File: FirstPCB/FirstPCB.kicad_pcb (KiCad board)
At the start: 2 copper layers, 50 x 30 mm, 5 parts, among them U1 STM32G0B1KETx

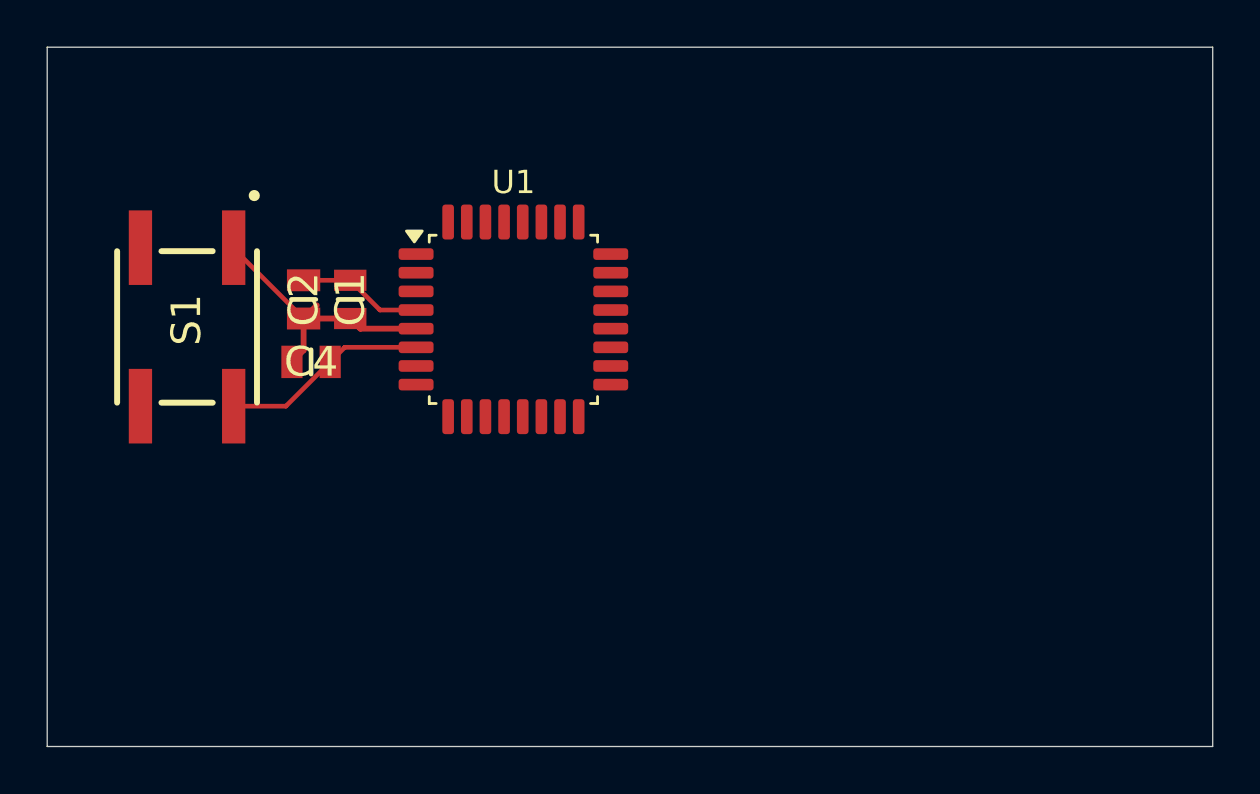
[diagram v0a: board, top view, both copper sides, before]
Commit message: added Voltage Regulator
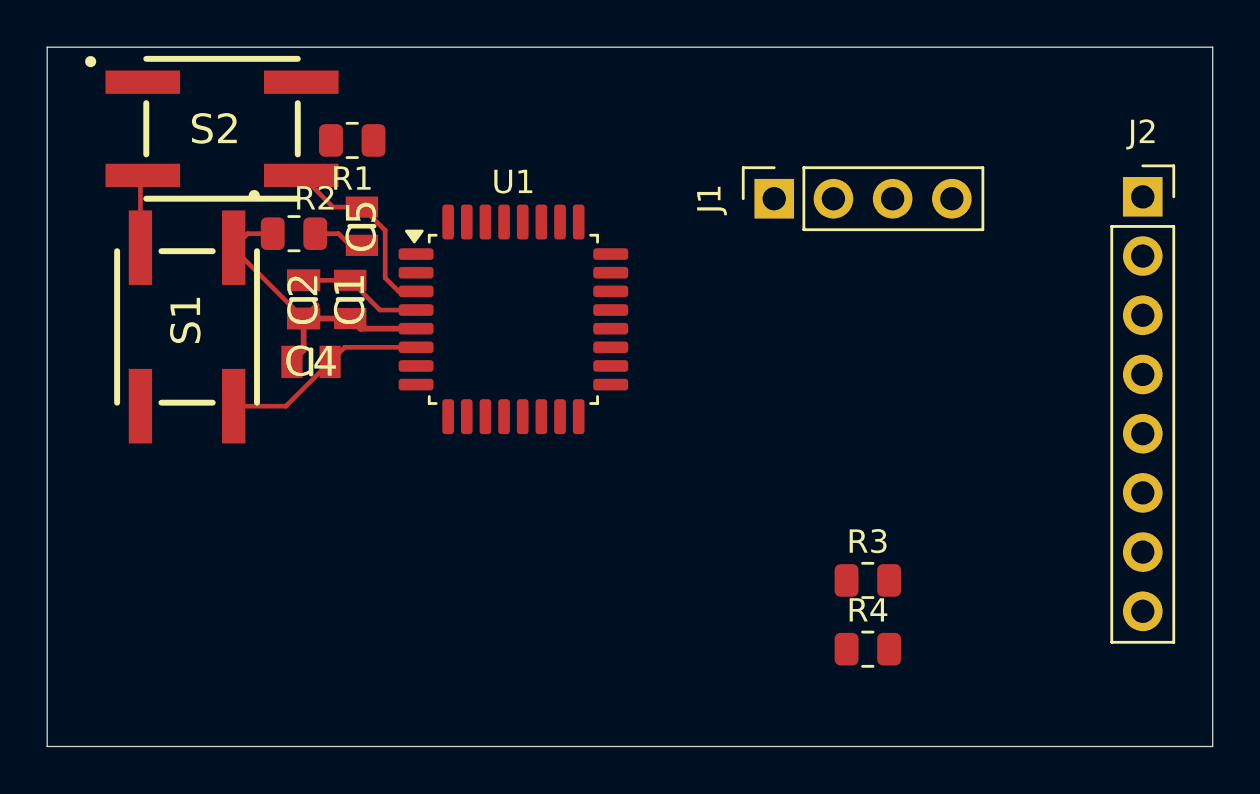
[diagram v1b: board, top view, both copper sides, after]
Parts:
- added C5: 100nF, SamacSys_Parts:CAPC2012X95N, F.Cu at (165.5, 89.7)
- added J1: Conn_01x04_Socket, Connector_PinSocket_2.54mm:PinSocket_1x04_P2.54mm_Vertical, F.Cu at (183.2, 88.5)
- added J2: Conn_01x08_Socket, Connector_PinSocket_2.54mm:PinSocket_1x08_P2.54mm_Vertical, F.Cu at (199.0, 88.4)
- added R1: 4.7 kOhm, Resistor_SMD:R_0805_2012Metric, F.Cu at (165.1, 86.0)
- added R2: 100 Ohm, Resistor_SMD:R_0805_2012Metric, F.Cu at (162.6, 90.0)
- added R3: 100 Ohm, Resistor_SMD:R_0805_2012Metric, F.Cu at (187.2, 104.9)
- added R4: 10 kOhm, Resistor_SMD:R_0805_2012Metric, F.Cu at (187.2, 107.8)
- added S2: EVQQ2B03W, SamacSys_Parts:EVQQ2, F.Cu at (159.5, 85.5)
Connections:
- U1 pad 23: unconnected-(U1-PA10/PA12-Pad23) -> Net-(U1-PA10/PA12)
- U1 pad 3: unconnected-(U1-PC15-Pad3) -> /BUTTON_CHANGE
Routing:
- net /BUTTON_CHANGE: track 0.00 -> 8.18 mm
- net GND: track 12.2 -> 17.2 mm
- net Net-(C5-Pad2): track 0.00 -> 2.21 mm
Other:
- board text added: "BUTTON_CHANGE"
- board text added: "N_RST"

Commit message: added sensor and schematic update
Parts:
- added R5: 1 kOhm, Resistor_SMD:R_0805_2012Metric, F.Cu at (186.7, 96.0)
- moved J1 1.69 mm to (181.5, 88.4), turned to 0 degrees
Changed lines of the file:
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@@
+		)
+	)
+	(footprint "Resistor_SMD:R_0805_2012Metric"
+		(layer "F.Cu")
+		(at 186.705 95.975)
+		(descr "Resistor SMD 0805 (2012 Metric), square (rectangular) end terminal, IPC-7351 nominal, (Body size source: IPC-SM-782 page 72, https://www.pcb-3d.com/wordpress/wp-content/uploads/ipc-sm-782a_amendment_1_and_2.pdf)")
+		(tags "resistor")
+		(property "Reference" "R5"
+			(at 0 -1.65 0)
+			(layer "F.SilkS")
+			(effects
+				(font
+					(size 1 1)
+					(thickness 0.15)
+				)
+			)
+		)
+		(property "Value" "1 kOhm"
+			(at 0 1.65 0)
+			(layer "F.Fab")
+			(effects
+				(font
+					(size 1 1)
+					(thickness 0.15)
+				)
+			)
+		)
+		(property "Datasheet" ""
+			(at 0 0 0)
+			(layer "F.Fab")
+			(hide yes)
+			(effects
+				(font
+					(size 1.27 1.27)
+				)
+			)
+		)
+		(property "Description" "Resistor"
+			(at 0 0 0)
+			(layer "F.Fab")
+			(hide yes)
+			(effects
+				(font
+					(size 1.27 1.27)
+				)
+			)
+		)
+		(property "KiLib_Generator" "SMD_2terminal_chip_molded"
+			(at 0 0 0)
+			(layer "F.SilkS")
+			(hide yes)
+			(effects
+				(font
+					(size 1 1)
+					(thickness 0.15)
+				)
+			)
+		)
+		(property ki_fp_filters "R_*")
+		(sheetname "/")
+		(sheetfile "FirstPCB.kicad_sch")
+		(units
+			(unit
+				(name "A")
+				(pins "1" "2")
+			)
+		)
+		(attr smd)
+		(duplicate_pad_numbers_are_jumpers no)
+		(fp_line
+			(start -0.227064 -0.735)
+			(end 0.227064 -0.735)
+			(stroke
+				(width 0.12)
+				(type solid)
+			)
+			(layer "F.SilkS")
+		)
+		(fp_line
+			(start -0.227064 0.735)
+			(end 0.227064 0.735)
+			(stroke
+				(width 0.12)
+				(type solid)
+			)
+			(layer "F.SilkS")
+		)
+		(fp_rect
+			(start -1.68 -0.95)
+			(end 1.68 0.95)
+			(stroke
+				(width 0.05)
+				(type solid)
+			)
+			(fill no)
+			(layer "F.CrtYd")
+		)
+		(fp_rect
+			(start -1 -0.625)
+			(end 1 0.625)
+			(stroke
+				(width 0.1)
+				(type solid)
+			)
+			(fill no)
+			(layer "F.Fab")
+		)
+		(fp_text user "${REFERENCE}"
+			(at 0 0 0)
+			(layer "F.Fab")
+			(effects
+				(font
+					(size 0.5 0.5)
+					(thickness 0.08)
+				)
+			)
+		)
+		(pad "1" smd roundrect
+			(at -0.9125 0)
+			(size 1.025 1.4)
+			(layers "F.Cu" "F.Mask" "F.Paste")
+			(roundrect_rratio 0.243902)
+			(net "+3.3V")
+			(pintype "passive")
+		)
+		(pad "2" smd roundrect
+			(at 0.9125 0)
+			(size 1.025 1.4)
+			(layers "F.Cu" "F.Mask" "F.Paste")
+			(roundrect_rratio 0.243902)
+			(net "Net-(LED1-Pad1)")
+			(pintype "passive")
+		)
+		(embedded_fonts no)
+		(model "${KICAD10_3DMODEL_DIR}/Resistor_SMD.3dshapes/R_0805_2012Metric.step"
+			(offset
+				(xyz 0 0 0)
+			)
+			(scale
+				(xyz 1 1 1)
+			)
+			(rotate
+				(xyz 0 0 0)
+			)
 		)
 	)
@@
 	(footprint "Connector_PinSocket_2.54mm:PinSocket_1x04_P2.54mm_Vertical"
 		(layer "F.Cu")
-		(at 183.19 88.5 90)
+		(at 181.5 88.42)
 		(descr "Through hole straight socket strip, 1x04, 2.54mm pitch, single row (from Kicad 4.0.7), script generated")
 		(tags "Through hole socket strip THT 1x04 2.54mm single row")
 		(property "Reference" "J1"
-			(at 0 -2.77 90)
+			(at 0 -2.77 0)
 			(layer "F.SilkS")
 			(effects
@@
 		)
 		(property "Value" "Conn_01x04_Socket"
-			(at 0 10.39 90)
+			(at 0 10.39 0)
 			(layer "F.Fab")
 			(effects
@@
 		)
 		(property "Datasheet" ""
-			(at 0 0 90)
+			(at 0 0 0)
 			(layer "F.Fab")
 			(hide yes)
@@
 		)
 		(property "Description" "Generic connector, single row, 01x04, script generated"
-			(at 0 0 90)
+			(at 0 0 0)
 			(layer "F.Fab")
 			(hide yes)
@@
 		)
 		(property "KiLib_Generator" "connector/pin_header_socket"
-			(at 0 0 90)
+			(at 0 0 0)
 			(layer "F.SilkS")
 			(hide yes)
@@
 		(duplicate_pad_numbers_are_jumpers no)
 		(fp_line
+			(start -1.33 1.27)
+			(end -1.33 8.95)
+			(stroke
+				(width 0.12)
+				(type solid)
+			)
+			(layer "F.SilkS")
+		)
+		(fp_line
+			(start -1.33 1.27)
+			(end 1.33 1.27)
+			(stroke
+				(width 0.12)
+				(type solid)
+			)
+			(layer "F.SilkS")
+		)
+		(fp_line
+			(start -1.33 8.95)
+			(end 1.33 8.95)
+			(stroke
+				(width 0.12)
+				(type solid)
+			)
+			(layer "F.SilkS")
+		)
+		(fp_line
+			(start 0 -1.33)
+			(end 1.33 -1.33)
+			(stroke
+				(width 0.12)
+				(type solid)
+			)
+			(layer "F.SilkS")
+		)
+		(fp_line
 			(start 1.33 -1.33)
 			(end 1.33 0)
@@
 		)
 		(fp_line
-			(start 0 -1.33)
-			(end 1.33 -1.33)
-			(stroke
-				(width 0.12)
-				(type solid)
-			)
-			(layer "F.SilkS")
-		)
-		(fp_line
 			(start 1.33 1.27)
 			(end 1.33 8.95)
@@
 		)
 		(fp_line
-			(start -1.33 1.27)
-			(end 1.33 1.27)
-			(stroke
-				(width 0.12)
-				(type solid)
-			)
-			(layer "F.SilkS")
-		)
-		(fp_line
-			(start -1.33 1.27)
-			(end -1.33 8.95)
-			(stroke
-				(width 0.12)
-				(type solid)
-			)
-			(layer "F.SilkS")
-		)
-		(fp_line
-			(start -1.33 8.95)
-			(end 1.33 8.95)
-			(stroke
-				(width 0.12)
-				(type solid)
-			)
-			(layer "F.SilkS")
+			(start -1.77 -1.77)
+			(end 1.77 -1.77)
+			(stroke
+				(width 0.05)
+				(type solid)
+			)
+			(layer "F.CrtYd")
+		)
+		(fp_line
+			(start -1.77 9.39)
+			(end -1.77 -1.77)
+			(stroke
+				(width 0.05)
+				(type solid)
+			)
+			(layer "F.CrtYd")
 		)
 		(fp_line
@@
 		)
 		(fp_line
-			(start -1.77 -1.77)
-			(end 1.77 -1.77)
-			(stroke
-				(width 0.05)
-				(type solid)
-			)
-			(layer "F.CrtYd")
-		)
-		(fp_line
 			(start 1.77 9.39)
 			(end -1.77 9.39)
@@
 		)
 		(fp_line
-			(start -1.77 9.39)
-			(end -1.77 -1.77)
-			(stroke
-				(width 0.05)
-				(type solid)
-			)
-			(layer "F.CrtYd")
+			(start -1.27 -1.27)
+			(end 0.635 -1.27)
+			(stroke
+				(width 0.1)
+				(type solid)
+			)
+			(layer "F.Fab")
+		)
+		(fp_line
+			(start -1.27 8.89)
+			(end -1.27 -1.27)
+			(stroke
+				(width 0.1)
+				(type solid)
+			)
+			(layer "F.Fab")
 		)
 		(fp_line
@@
 		)
 		(fp_line
-			(start -1.27 -1.27)
-			(end 0.635 -1.27)
-			(stroke
-				(width 0.1)
-				(type solid)
-			)
-			(layer "F.Fab")
-		)
-		(fp_line
 			(start 1.27 -0.635)
 			(end 1.27 8.89)
@@
 			(layer "F.Fab")
 		)
-		(fp_line
-			(start -1.27 8.89)
-			(end -1.27 -1.27)
-			(stroke
-				(width 0.1)
-				(type solid)
-			)
-			(layer "F.Fab")
-		)
 		(fp_text user "${REFERENCE}"
-			(at 0 3.81 0)
+			(at 0 3.81 90)
 			(layer "F.Fab")
 			(effects
@@
 		)
 		(pad "1" thru_hole rect
-			(at 0 0 90)
+			(at 0 0)
 			(size 1.7 1.7)
 			(drill 1)
@@
 		)
 		(pad "2" thru_hole circle
-			(at 0 2.54 90)
+			(at 0 2.54)
 			(size 1.7 1.7)
 			(drill 1)
@@
 		)
 		(pad "3" thru_hole circle
-			(at 0 5.08 90)
+			(at 0 5.08)
 			(size 1.7 1.7)
 			(drill 1)
@@
 		)
 		(pad "4" thru_hole circle
-			(at 0 7.62 90)
+			(at 0 7.62)
 			(size 1.7 1.7)
 			(drill 1)

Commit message: shematic finished
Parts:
- removed the J1 at (181.5, 88.4)
- removed the J2 at (199.0, 88.4)
- added C3: 22uF, CL21A226MQQNNNE:CAPC2012X140N, F.Cu at (124.2, 75.0)
- added C6: 22uF, CL21A226MQQNNNE:CAPC2012X140N, F.Cu at (124.2, 78.0)
- added IC1: ENS210-LQFM, SamacSys_Parts:SON95P200X200X80-5N, F.Cu at (79.5, 99.6)
- added J1: Conn_01x04_Socket, Connector_PinSocket_2.54mm:PinSocket_1x04_P2.54mm_Vertical, F.Cu at (141.0, 96.3)
- added J1: Conn_01x08_Socket, Connector_PinSocket_2.54mm:PinSocket_1x08_P2.54mm_Vertical, F.Cu at (63.3, 87.8)
- added J2: Conn_01x04_Socket, Connector_PinSocket_2.54mm:PinSocket_1x04_P2.54mm_Vertical, F.Cu at (67.9, 87.8)
- added J2: Conn_01x08_Socket, Connector_PinSocket_2.54mm:PinSocket_1x08_P2.54mm_Vertical, F.Cu at (194.5, 101.3)
- added J3: Conn_01x04_Socket, Connector_PinSocket_2.54mm:PinSocket_1x04_P2.54mm_Vertical, F.Cu at (72.5, 87.8)
- added J5: Conn_01x04_Socket, Connector_PinSocket_2.54mm:PinSocket_1x04_P2.54mm_Vertical, F.Cu at (77.1, 87.8)
- added LED1: Green 0805, CRG1206F470R:RESC3115X65N, F.Cu at (110.8, 72.1)
- added R6: 4.7 kOhm, Resistor_SMD:R_0805_2012Metric, F.Cu at (81.6, 87.0)
- added R7: 4.7 kOhm, Resistor_SMD:R_0805_2012Metric, F.Cu at (81.6, 89.9)
- added R8: 5.1 kOhm, Resistor_SMD:R_0805_2012Metric, F.Cu at (81.6, 92.9)
- added R9: 5.1 kOhm, Resistor_SMD:R_0805_2012Metric, F.Cu at (81.6, 95.8)
- added U2: AMS1117-3.3, Package_TO_SOT_SMD:SOT-223-3_TabPin2, F.Cu at (91.6, 63.3)
- added USB1: TYPE-C_6P, Connector_USB:USB_C_Receptacle_GCT_USB4135-GF-A_6P_TopMnt_Horizontal, F.Cu at (85.9, 107.4)
- moved S2 46.3 mm to (203.5, 100.0), turned to 90 degrees
- moved S1 46.3 mm to (203.5, 85.4)
- moved R3 30.8 mm to (156.9, 110.4)
- moved R5 30.8 mm to (156.4, 101.5)
- moved R4 30.8 mm to (156.9, 113.3)
- moved C2 27.2 mm to (183.5, 75.0)
- moved C1 23.2 mm to (181.0, 76.0)
- moved C4 19.8 mm to (166.8, 76.0)
- moved C5 16.2 mm to (176.5, 77.8)
- moved R2 16.0 mm to (147.1, 86.0)
- moved R1 12.3 mm to (171.4, 75.5)
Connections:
- R3 pad 1: Net-(U1-PA10/PA12) -> /DISP_LED
- U1 pad 10: unconnected-(U1-PA3-Pad10) -> /UART_RX
- U1 pad 11: unconnected-(U1-PA4-Pad11) -> /ADC_IN_4
- U1 pad 12: unconnected-(U1-PA5-Pad12) -> /ADC_IN_5
- U1 pad 13: unconnected-(U1-PA6-Pad13) -> /SENSOR_SDA
- U1 pad 14: unconnected-(U1-PA7-Pad14) -> /SENSOR_SCL
- U1 pad 20: unconnected-(U1-PC6-Pad20) -> /DISP_LED
- U1 pad 21: unconnected-(U1-PA10/UCPD1_DBCC2-Pad21) -> /DISP_RES
- U1 pad 22: unconnected-(U1-PA9/PA11-Pad22) -> /DISP_DC
- U1 pad 23: Net-(U1-PA10/PA12) -> unconnected-(U1-PA10/PA12-Pad23)
- U1 pad 24: unconnected-(U1-PA13-Pad24) -> /SW_DIO
- U1 pad 25: unconnected-(U1-PA14-Pad25) -> /SW_CLK
- U1 pad 26: unconnected-(U1-PA15-Pad26) -> /DISP_CS
- U1 pad 27: unconnected-(U1-PB3-Pad27) -> /DISP_MISO
- U1 pad 28: unconnected-(U1-PB4-Pad28) -> /SD_CS
- U1 pad 29: unconnected-(U1-PB5-Pad29) -> /DISP_MOSI
- U1 pad 30: unconnected-(U1-PB6-Pad30) -> /SD_MISO
- U1 pad 31: unconnected-(U1-PB7-Pad31) -> /SD_MOSI
- U1 pad 32: unconnected-(U1-PB8-Pad32) -> /SD_SCK
- U1 pad 9: unconnected-(U1-PA2-Pad9) -> /UART_TX
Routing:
- net GND: track 17.2 -> 0.00 mm
- net /NRST: track 8.87 -> 0.00 mm
- net /BUTTON_CHANGE: track 8.18 -> 0.75 mm
- net +3.3V: track 5.74 -> 0.00 mm
- net Net-(C5-Pad2): track 2.21 -> 0.00 mm
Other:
- board size 50 x 30 mm -> 71 x 40 mm
- board text removed: "BUTTON_CHANGE"

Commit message: before routing
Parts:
- removed the J1 at (141.0, 96.3)
- removed the J2 at (194.5, 101.3)
- added ?: LOGO, LOGO, F.Cu at (139.5, 119.0)
- J3: value Conn_01x04_Socket -> SWD
- J4: renamed from J5; value Conn_01x04_Socket -> UART & ADC
- U1: value STM32G0B1KETx -> STM32G0B1
- moved U2 102.3 mm to (142.5, 152.0), turned to 180 degrees
- moved S1 102.1 mm to (145.6, 169.5), turned to 0 degrees
- moved C5 100.1 mm to (126.5, 164.5), turned to 90 degrees
- moved J1 99.7 mm to (130.5, 161.5), turned to 90 degrees
- moved S2 99.4 mm to (132.5, 169.5), turned to 180 degrees
- moved R1 98.7 mm to (129.9, 165.0)
- moved J3 95.0 mm to (156.0, 133.0)
- moved R8 92.0 mm to (149.0, 155.5), turned to 90 degrees
- moved C4 91.9 mm to (152.0, 166.7), turned to 90 degrees
- moved LED1 88.3 mm to (135.0, 157.0), turned to 90 degrees
- moved R9 87.8 mm to (149.0, 152.0), turned to -90 degrees
- moved USB1 82.8 mm to (156.0, 151.5), turned to 90 degrees
- moved C6 82.1 mm to (142.6, 158.0)
- moved C2 81.8 mm to (140.3, 144.5), turned to 0 degrees
- moved R7 81.4 mm to (146.9, 138.5), turned to 180 degrees
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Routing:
- net /BUTTON_CHANGE: track 0.75 -> 0.00 mm
- added copper zone on B.Cu, net GND
- added copper zone on F.Cu, net GND
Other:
- board size 71 x 40 mm -> 40.5 x 71 mm
- board text added: "Author: Granitovich"
- board text removed: "N_RST"

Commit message: minimal routing
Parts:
- removed ?: LOGO, LOGO
- moved C4 6.40 mm to (145.8, 165.0), turned to 180 degrees
- moved C3 1.21 mm to (149.0, 147.6), turned to 90 degrees
- moved U2 0.50 mm to (142.0, 152.0)
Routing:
- net GND: track 0.00 -> 50.8 mm
- net VBUS: track 0.00 -> 13.7 mm
- net +3.3V: track 0.00 -> 7.42 mm
- net Net-(USB1-CC1): track 0.00 -> 5.04 mm
- net Net-(USB1-CC2): track 0.00 -> 4.76 mm
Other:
- board text added: "N_RST"
- board text removed: "Author: Granitovich"

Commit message: finished routing
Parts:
- moved R1 0.18 mm to (130.1, 165.0)
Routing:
- net GND: track 50.8 -> 139.0 mm, vias 0 -> 6
- net +3.3V: track 7.42 -> 85.1 mm, vias 0 -> 5
- net /SD_SCK: track 0.00 -> 59.9 mm, vias 0 -> 2
- net /NRST: track 0.00 -> 48.4 mm, vias 0 -> 4
- net /DISP_RES: track 0.00 -> 41.9 mm, vias 0 -> 1
- net /SD_MISO: track 0.00 -> 39.9 mm, vias 0 -> 2
- net /BUTTON_CHANGE: track 0.00 -> 37.2 mm
- net /SD_MOSI: track 0.00 -> 36.0 mm, vias 0 -> 2
- net /ADC_IN_4: track 0.00 -> 34.1 mm, vias 0 -> 1
- net /UART_TX: track 0.00 -> 33.8 mm, vias 0 -> 2
- net /SD_CS: track 0.00 -> 33.1 mm, vias 0 -> 2
- net /SW_CLK: track 0.00 -> 32.6 mm, vias 0 -> 2
- net /DISP_DC: track 0.00 -> 32.2 mm, vias 0 -> 4
- net /DISP_CS: track 0.00 -> 32.0 mm, vias 0 -> 1
- net /DISP_LED: track 0.00 -> 30.5 mm, vias 0 -> 2
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- removed copper zone on B.Cu, net GND
- removed copper zone on F.Cu, net GND
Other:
- board text added: "BUTTON_CHANGE"
- board text added: "N_RESET"
- board text removed: "N_RST"

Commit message: update gerber
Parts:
- added SmartAvtomatic: LOGO, LOGO, F.Cu at (151.5, 117.5)
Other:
- board text added: "Created by Granitovich"

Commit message: design finished, ordered pcb
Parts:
- removed SmartAvtomatic: LOGO, LOGO
- added ?: LOGO, LOGO, F.Cu at (149.5, 121.0)
- J3: value SWD -> Conn_01x04_Socket
- J4: value UART & ADC -> Conn_01x04_Socket
- moved J4 33.5 mm to (156.0, 133.2)
- moved J3 33.5 mm to (122.5, 133.0)
- moved R4 23.2 mm to (149.9, 164.5), turned to 180 degrees
- moved LED1 21.9 mm to (156.5, 161.5), turned to 0 degrees
- moved J1 17.6 mm to (148.0, 161.5), turned to -90 degrees
- moved R3 17.0 mm to (148.0, 157.9)
- moved R5 13.6 mm to (152.1, 161.5), turned to 0 degrees
- moved R2 10.0 mm to (130.9, 165.0), turned to 0 degrees
- moved C1 8.87 mm to (135.2, 145.0)
- moved C6 7.76 mm to (147.0, 151.6), turned to -90 degrees
- moved C4 7.37 mm to (153.0, 166.7), turned to 90 degrees
- moved C2 5.35 mm to (135.2, 143.0), turned to 180 degrees
- moved R1 5.32 mm to (126.1, 161.5)
- moved U1 4.03 mm to (135.0, 136.0)
- moved U2 2.14 mm to (140.8, 150.2)
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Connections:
- J2 pad 1: /SD_SCK -> /SD_CS
- J2 pad 2: /SD_MISO -> /SD_MOSI
- J2 pad 3: /SD_MOSI -> /SD_MISO
- J2 pad 4: /SD_CS -> /SD_SCK
- J3 pad 1: +3.3V -> /SW_DIO
- J3 pad 2: /SW_DIO -> /SW_CLK
- J3 pad 3: /SW_CLK -> +3.3V
- U1 pad 20: /DISP_LED -> unconnected-(U1-PC6-Pad20)
- U1 pad 27: /DISP_MISO -> /DISP_SCK
- U1 pad 8: unconnected-(U1-PA1-Pad8) -> /DISP_LED
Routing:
- net /DISP_SCK: track 0.00 -> 46.8 mm, vias 0 -> 2
- net GND: track 139.0 -> 162.5 mm, vias 6 -> 4
- net /SW_CLK: track 32.6 -> 9.29 mm, vias 2 -> 0
- net /SW_DIO: track 26.7 -> 10.2 mm
- net /UART_TX: track 33.8 -> 17.7 mm, vias 2 -> 1
- net /DISP_DC: track 32.2 -> 47.0 mm, vias 4 -> 2
- net /ADC_IN_4: track 34.1 -> 19.6 mm, vias 1 -> 2
- net +3.3V: track 85.1 -> 98.7 mm, vias 5 -> 4
- net /SD_SCK: track 59.9 -> 49.8 mm
- net /DISP_MOSI: track 27.3 -> 36.0 mm
- net /ADC_IN_5: track 26.2 -> 18.7 mm, vias 1 -> 2
- net /DISP_LED: track 30.5 -> 23.5 mm
- net /DISP_CS: track 32.0 -> 37.0 mm, vias 1 -> 2
- net /SENSOR_SDA: track 5.03 -> 9.23 mm
- net /SENSOR_SCL: track 5.22 -> 9.00 mm
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- added copper zone on B.Cu, net GND
- added copper zone on F.Cu, net GND
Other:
- board text added: "Author: Granitovich"
- board text removed: "BUTTON_CHANGE"
- board text removed: "Created by Granitovich"
- board text removed: "N_RESET"
